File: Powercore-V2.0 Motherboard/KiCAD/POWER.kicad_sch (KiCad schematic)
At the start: 37 parts, among them U10 UA78M33CKVURG3, U12 UA78M05CDCYR, U9 LM5169FDDAR

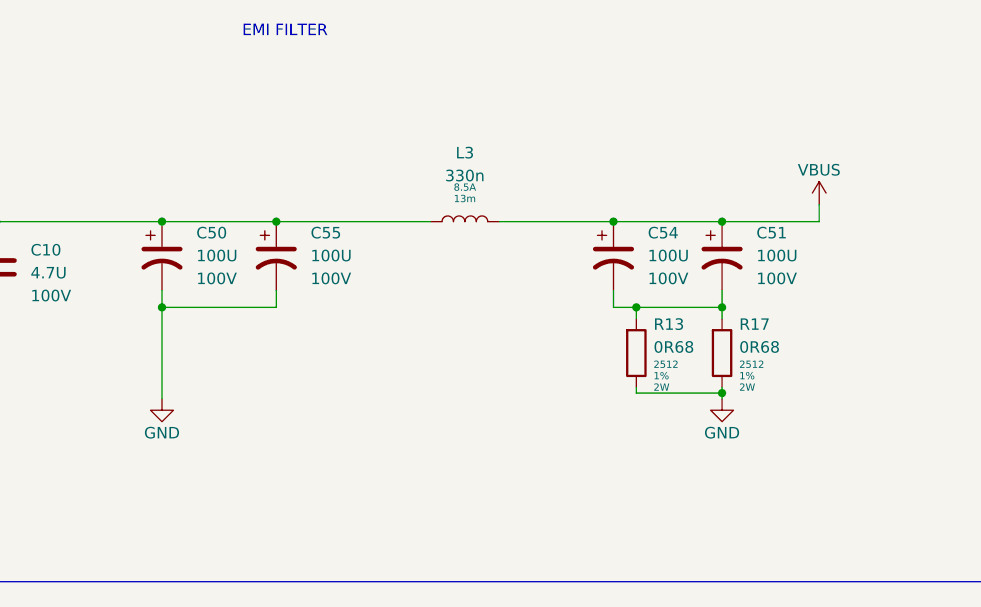
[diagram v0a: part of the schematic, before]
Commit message: Attempt to mitigate failure mode
Replaced gate driver
Replaced FETs
Added input filter to gate driver
Removed input PI filter
Updated control timing to reduce initial metastability
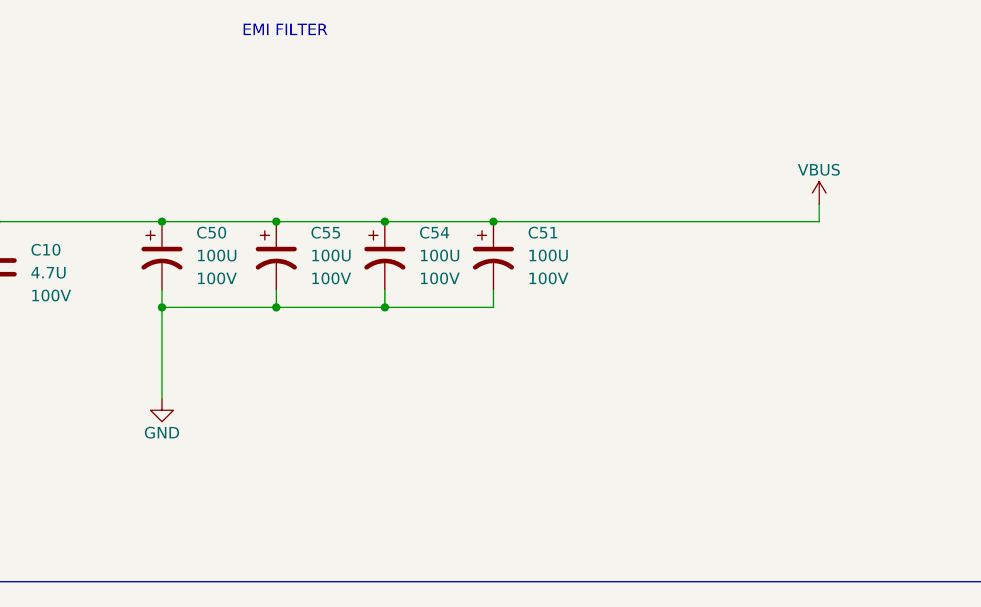
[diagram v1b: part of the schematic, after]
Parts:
- removed L3: 330n, Inductor_SMD:L_1210_3225Metric, symbol POWER_INDUCTORS:SRP3212A-R33M
- removed R13, R17: 0R68, SMD_RESISTORS:CSRN2512, symbol POWER_RESISTOR:0R68_2512_2W
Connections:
- net VDC is gone; now on net VBUS: C10.1, C10.1, C50.1, C55.1, C72.1, C72.1
- net GND: now also C51.2, C54.2
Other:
- moved on the sheet: C51, C54
